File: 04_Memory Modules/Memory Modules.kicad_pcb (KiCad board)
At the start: 2 copper layers, 100 x 100 mm, 55 parts, among them J1 Data bus, J2 Address bus 1, J3 Address bus 2, J4 Input 1, J5 Input 2, Q1 PN2222A, U1 74LS139, U10 CY7C199, U11 28C256, U2 74LS08, U3 74LS193, U4 74LS245, U5 74LS193, U6 74LS193, U7 74LS245, U8 74LS193, U9 CY7C199

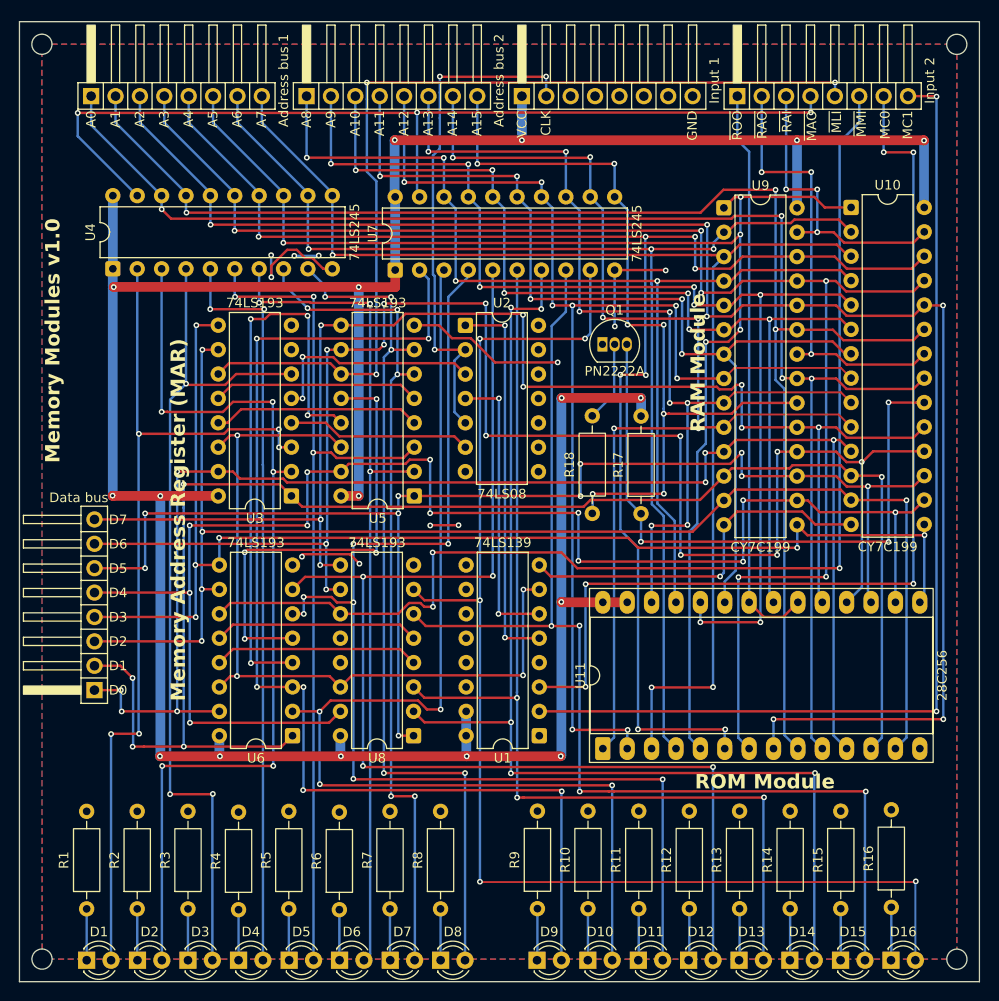
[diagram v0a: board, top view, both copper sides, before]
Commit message: Last revision of the cpu, all boards have been ordered. Implementation to be tested and documented in following commits.
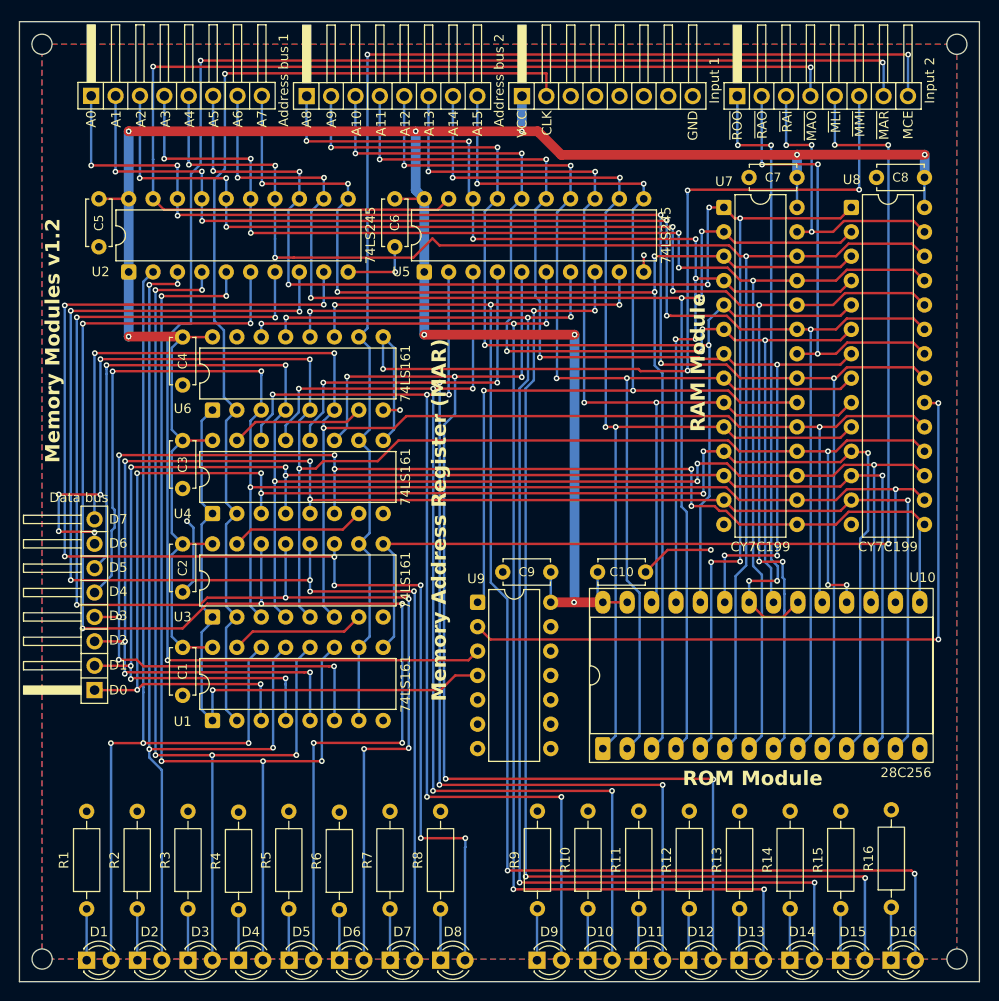
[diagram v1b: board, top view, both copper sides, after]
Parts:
- removed Q1: PN2222A, Package_TO_SOT_THT:TO-92_Inline
- removed R17: 1K, Resistor_THT:R_Axial_DIN0207_L6.3mm_D2.5mm_P10.16mm_Horizontal
- removed R18: 10K, Resistor_THT:R_Axial_DIN0207_L6.3mm_D2.5mm_P10.16mm_Horizontal
- removed the REF** at (147.7, 140.7)
- removed the REF** at (52.3, 45.4)
- removed the REF** at (147.6, 45.4)
- removed the REF** at (52.4, 140.6)
- removed the U2 at (96.4, 74.6)
- removed the U5 at (91.1, 92.4)
- removed the U8 at (91.1, 117.4)
- added C1: 100n, Capacitor_THT:C_Disc_D4.7mm_W2.5mm_P5.00mm, F.Cu at (67.0, 108.2)
- added C10: 10nF, Capacitor_THT:C_Disc_D4.7mm_W2.5mm_P5.00mm, F.Cu at (110.2, 100.3)
- added C2: 100n, Capacitor_THT:C_Disc_D4.7mm_W2.5mm_P5.00mm, F.Cu at (67.0, 97.4)
- added C3: 100n, Capacitor_THT:C_Disc_D4.7mm_W2.5mm_P5.00mm, F.Cu at (67.0, 86.6)
- added C4: 100n, Capacitor_THT:C_Disc_D4.7mm_W2.5mm_P5.00mm, F.Cu at (67.0, 75.8)
- added C5: 100n, Capacitor_THT:C_Disc_D4.7mm_W2.5mm_P5.00mm, F.Cu at (58.3, 61.5)
- added C6: 100n, Capacitor_THT:C_Disc_D4.7mm_W2.5mm_P5.00mm, F.Cu at (89.1, 61.5)
- added C7: 100n, Capacitor_THT:C_Disc_D4.7mm_W2.5mm_P5.00mm, F.Cu at (131.0, 59.2)
- added C8: 100n, Capacitor_THT:C_Disc_D4.7mm_W2.5mm_P5.00mm, F.Cu at (144.3, 59.2)
- added C9: 100n, Capacitor_THT:C_Disc_D4.7mm_W2.5mm_P5.00mm, F.Cu at (105.3, 100.3)
- added REF**: MountingHole_2.1mm, MountingHole:MountingHole_2.1mm, F.Cu at (52.4, 140.6)
- added REF**: MountingHole_2.1mm, MountingHole:MountingHole_2.1mm, F.Cu at (147.7, 45.4)
- added REF**: MountingHole_2.1mm, MountingHole:MountingHole_2.1mm, F.Cu at (52.4, 45.4)
- added REF**: MountingHole_2.1mm, MountingHole:MountingHole_2.1mm, F.Cu at (147.7, 140.6)
- added U4: 74LS161, Package_DIP:DIP-16_W7.62mm, F.Cu at (70.1, 94.2)
- added U9: 74LS04, Package_DIP:DIP-14_W7.62mm, F.Cu at (97.7, 103.5)
- U1: value 74LS139 -> 74LS161
- U3, U6: value 74LS193 -> 74LS161
- moved U6 34.9 mm to (70.1, 83.5), turned to 90 degrees
- moved U1 34.1 mm to (70.1, 115.8), turned to 90 degrees
- moved U3 15.1 mm to (70.1, 105.0), turned to 90 degrees
- moved U5 3.04 mm to (92.2, 69.1)
- moved U2 1.68 mm to (61.4, 69.1)
- renumbered U11 to U10, U4 to U2, U7 to U5, U9 to U7, U10 to U8
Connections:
- net /A0 renamed A0
- net /A1 renamed A1
- net /A10 renamed A10
- net /A11 renamed A11
- net /A12 renamed A12
- net /A13 renamed A13
- net /A14 renamed A14
- net /A15 renamed A15
- net /A2 renamed A2
- net /A3 renamed A3
- net /A4 renamed A4
- net /A5 renamed A5
- net /A6 renamed A6
- net /A7 renamed A7
- net /A8 renamed A8
- net /A9 renamed A9
- net /~{MAO} renamed ~{MAO}
- net /~{RAI} renamed ~{RAI}
- net /~{RAO} renamed ~{RAO}
- net /~{ROO} renamed ~{ROO}
- J1 pad 1: /D0 -> D0
- J1 pad 2: /D1 -> D1
- J1 pad 3: /D2 -> D2
- J1 pad 4: /D3 -> D3
- J1 pad 5: /D4 -> D4
- J1 pad 6: /D5 -> D5
- J1 pad 7: /D6 -> D6
- J1 pad 8: /D7 -> D7
- J4 pad 1: /VCC -> VCC
- J4 pad 2: /CLK -> CLK
- J4 pad 8: /GND -> GND
- J5 pad 5: /~{MLI} -> ~{MLI}
- J5 pad 6: /~{MMI} -> ~{MMI}
- J5 pad 7: /MC0 -> MAR
- J5 pad 8: /MC1 -> MCE
- R1 pad 2: /GND -> GND
- R10 pad 2: /GND -> GND
- R11 pad 2: /GND -> GND
- R12 pad 2: /GND -> GND
- R13 pad 2: /GND -> GND
- R14 pad 2: /GND -> GND
- R15 pad 2: /GND -> GND
- R16 pad 2: /GND -> GND
- R2 pad 2: /GND -> GND
- R3 pad 2: /GND -> GND
- R4 pad 2: /GND -> GND
- R5 pad 2: /GND -> GND
- R6 pad 2: /GND -> GND
- R7 pad 2: /GND -> GND
- R8 pad 2: /GND -> GND
- R9 pad 2: /GND -> GND
- U1 pad 1: /GND -> Net-(U1-~{MR})
- U1 pad 10: unconnected-(U1B-O2-Pad10) -> MCE
- U1 pad 11: unconnected-(U1B-O1-Pad11) -> Net-(D4-A)
- U1 pad 12: unconnected-(U1B-O0-Pad12) -> Net-(D3-A)
- U1 pad 13: /GND -> Net-(D2-A)
- U1 pad 14: /GND -> Net-(D1-A)
- U1 pad 15: /VCC -> Net-(U1-TC)
- U1 pad 16: /VCC -> VCC
- U1 pad 2: /MC1 -> CLK
- U1 pad 3: /MC0 -> D0
- U1 pad 4: unconnected-(U1A-O0-Pad4) -> D1
- U1 pad 5: Net-(U1A-O1) -> D2
- U1 pad 6: Net-(U1A-O2) -> D3
- U1 pad 7: Net-(U1A-O3) -> MCE
- U1 pad 8: /GND -> GND
- U1 pad 9: unconnected-(U1B-O3-Pad9) -> ~{MLI}
- U10 pad 11: /D0 -> D0
- U10 pad 12: /D1 -> D1
- U10 pad 13: /D2 -> D2
- U10 pad 14: /GND -> GND
- U10 pad 15: /D3 -> D3
- U10 pad 16: /D4 -> D4
- U10 pad 17: /D5 -> D5
- U10 pad 18: /D6 -> D6
- U10 pad 19: /D7 -> D7
- U10 pad 27: /VCC -> VCC
- U10 pad 28: /VCC -> VCC
- U2 pad 1: /VCC -> VCC
- U2 pad 10: /GND -> GND
- U2 pad 20: /VCC -> VCC
- U3 pad 1: /D1 -> Net-(U1-~{MR})
- U3 pad 10: /D2 -> MCE
- U3 pad 11: /~{MLI} -> Net-(D8-A)
- U3 pad 12: Net-(U3-~{CO}) -> Net-(D7-A)
- U3 pad 13: Net-(U3-~{BO}) -> Net-(D6-A)
- U3 pad 14: Net-(U1A-O3) -> Net-(D5-A)
- U3 pad 15: /D0 -> Net-(U3-TC)
- U3 pad 16: /VCC -> VCC
- U3 pad 2: Net-(D2-A) -> CLK
- U3 pad 3: Net-(D1-A) -> D4
- U3 pad 4: Net-(U3-DOWN) -> D5
- U3 pad 5: Net-(U3-UP) -> D6
- U3 pad 6: Net-(D3-A) -> D7
- U3 pad 7: unconnected-(U3-QD-Pad7) -> Net-(U1-TC)
- U3 pad 8: /GND -> GND
- U3 pad 9: /D3 -> ~{MLI}
- U5 pad 1: /VCC -> VCC
- U5 pad 10: /GND -> GND
- U5 pad 20: /VCC -> VCC
- U6 pad 1: /D1 -> Net-(U1-~{MR})
- U6 pad 10: /D2 -> MCE
- U6 pad 11: /~{MMI} -> Net-(D16-A)
- U6 pad 12: Net-(U6-~{CO}) -> Net-(D15-A)
- U6 pad 13: Net-(U6-~{BO}) -> Net-(D14-A)
- U6 pad 14: Net-(U1A-O3) -> Net-(D13-A)
- U6 pad 15: /D0 -> unconnected-(U6-TC-Pad15)
- U6 pad 16: /VCC -> VCC
- U6 pad 2: Net-(D10-A) -> CLK
- U6 pad 3: Net-(D9-A) -> D4
- U6 pad 4: Net-(U5-~{BO}) -> D5
- U6 pad 5: Net-(U5-~{CO}) -> D6
- U6 pad 6: Net-(D11-A) -> D7
- U6 pad 7: Net-(D12-A) -> Net-(U4-TC)
- U6 pad 8: /GND -> GND
- U6 pad 9: /D3 -> ~{MMI}
- U7 pad 11: /D0 -> D0
- U7 pad 12: /D1 -> D1
- U7 pad 13: /D2 -> D2
- U7 pad 14: /GND -> GND
- U7 pad 15: /D3 -> D3
- U7 pad 16: /D4 -> D4
- U7 pad 17: /D5 -> D5
- U7 pad 18: /D6 -> D6
- U7 pad 19: /D7 -> D7
- U7 pad 28: /VCC -> VCC
- U8 pad 11: /D0 -> D0
- U8 pad 12: /D1 -> D1
- U8 pad 13: /D2 -> D2
- U8 pad 14: /GND -> GND
- U8 pad 15: /D3 -> D3
- U8 pad 16: /D4 -> D4
- U8 pad 17: /D5 -> D5
- U8 pad 18: /D6 -> D6
- U8 pad 19: /D7 -> D7
- U8 pad 28: /VCC -> VCC
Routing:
- net /VCC: track 316.7 -> 0.00 mm, vias 17 -> 0
- net VCC: track 0.00 -> 259.0 mm, vias 0 -> 9
- net MAR: track 0.00 -> 171.9 mm, vias 0 -> 3
- net /D6: track 170.6 -> 0.00 mm, vias 12 -> 0
- net D2: track 0.00 -> 164.1 mm, vias 0 -> 7
- net D6: track 0.00 -> 162.3 mm, vias 0 -> 10
- net D0: track 0.00 -> 161.5 mm, vias 0 -> 8
- net /D1: track 160.9 -> 0.00 mm, vias 5 -> 0
- net D1: track 0.00 -> 159.5 mm, vias 0 -> 7
- net /D4: track 156.6 -> 0.00 mm, vias 12 -> 0
- net D3: track 0.00 -> 156.3 mm, vias 0 -> 8
- net D7: track 0.00 -> 153.6 mm, vias 0 -> 4
- net D5: track 0.00 -> 153.0 mm, vias 0 -> 6
- net D4: track 0.00 -> 149.5 mm, vias 0 -> 4
- net /D0: track 147.8 -> 0.00 mm, vias 7 -> 0
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- added copper zone on B.Cu, net GND
- added copper zone on F.Cu, net GND
- removed copper zone on B.Cu, net /GND
- removed copper zone on F.Cu, net /GND
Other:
- board text added: "Memory Modules v1.2"
- board text removed: "Memory Modules v1.0"

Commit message: Update 10-01-2026 - Fixed bug on program counter - Fist ISA review, still in draft - Added missing mounting holes on memory modules
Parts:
- added TP1: GND, TestPoint:TestPoint_Loop_D3.50mm_Drill0.9mm_Beaded, F.Cu at (146.9, 131.6)
- added TP2: VCC, TestPoint:TestPoint_Loop_D3.50mm_Drill0.9mm_Beaded, F.Cu at (146.9, 126.3)
- added TP3: CLK, TestPoint:TestPoint_Loop_D3.50mm_Drill0.9mm_Beaded, F.Cu at (55.5, 119.4)
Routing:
- net VCC: track 259.0 -> 315.6 mm, vias 9 -> 11
- net CLK: track 107.5 -> 127.6 mm, vias 1 -> 2
